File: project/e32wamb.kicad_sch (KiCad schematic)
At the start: 29 parts, among them J1 2060-452_998-404, J2 Conn_01x04, J3 Conn_01x03, Q1 AO3400, Q2 AO3400, Q3 AO3400, Q4 AO3400, Q5 AO3400, SW1 TS-1187A-B-A-B, U1 AP63203WU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

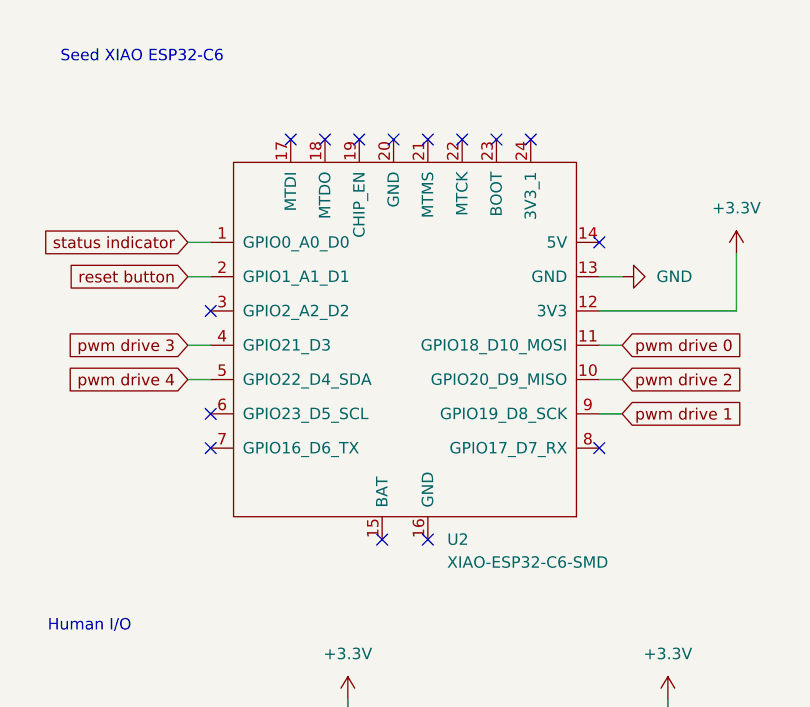
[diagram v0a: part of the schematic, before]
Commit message: Update xiao (don't place, add ds+source)
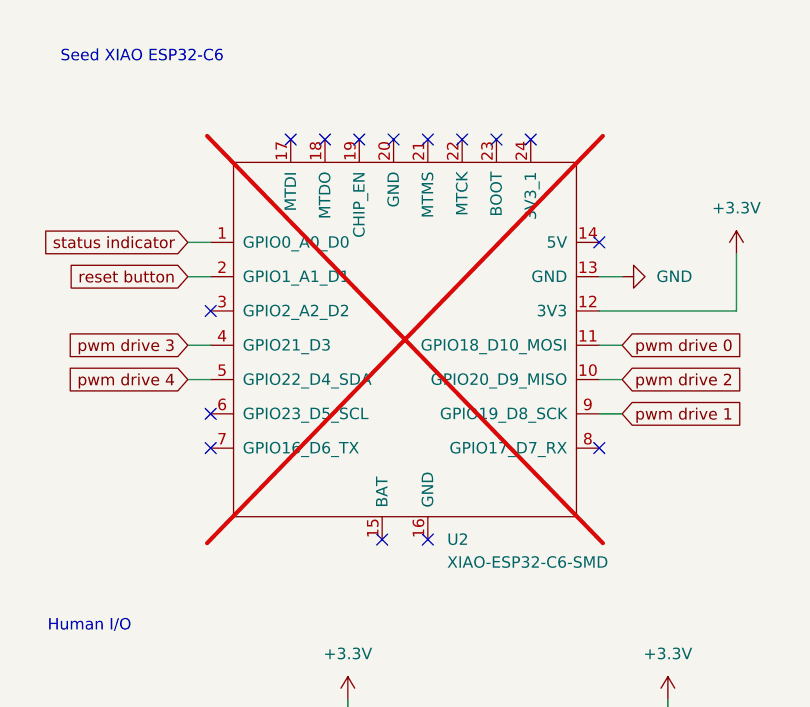
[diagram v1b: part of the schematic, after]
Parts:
- U2: Source (none) -> https://www.seeedstudio.com/Seeed-Studio-XIAO-ESP32C6-p-588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; now not fitted
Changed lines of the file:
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@@
 		(in_bom yes)
 		(on_board yes)
-		(dnp no)
+		(dnp yes)
 		(fields_autoplaced yes)
 		(property "Reference" "U2"
@@
 			)
 		)
-		(property "Datasheet" ""
+		(property "Datasheet" "https://files.seeedstudio.com/wiki/SeeedStudio-XIAO-ESP32C6/res/esp32-c6_datasheet_en.pdf"
 			(at 223.52 46.99 0)
 			(effects
@@
 			(at 232.41 52.07 0)
 			(effects
+				(font
+					(size 1.27 1.27)
+				)
+				(hide yes)
+			)
+		)
+		(property "Source" "https://www.seeedstudio.com/Seeed-Studio-XIAO-ESP32C6-p-5884.html"
+			(at 232.41 52.07 0)
+			(effects

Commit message: Add ohm symbol to all Rs, add license info
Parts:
- R1: value 10K -> 10kΩ
- R10, R12, R4, R6, R8: value 10k -> 10kΩ
- R11, R3, R5, R7, R9: value 390 -> 390Ω
- R2: value 0 -> 0Ω
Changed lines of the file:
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@@
 		(date "2025-04-05")
 		(company "wejn.org")
+		(comment 1 "Licensed under CC BY-SA 4.0")
+		(comment 2 "Open Source Hardware")
 	)
 	(text "Human I/O"
@@
 			)
 		)
-		(property "Value" "0"
+		(property "Value" "0Ω"
 			(at 213.36 96.52 90)
 			(effects
@@
 			)
 		)
-		(property "Value" "10k"
+		(property "Value" "10kΩ"
 			(at 35.56 144.7799 0)
 			(effects
@@
 			)
 		)
-		(property "Value" "390"
+		(property "Value" "390Ω"
 			(at 74.93 96.5199 0)
 			(effects
@@
 			)
 		)
-		(property "Value" "10k"
+		(property "Value" "10kΩ"
 			(at 35.56 105.4099 0)
 			(effects
@@
 			)
 		)
-		(property "Value" "10k"
+		(property "Value" "10kΩ"
 			(at 74.93 144.7799 0)
 			(effects
@@
 			)
 		)
-		(property "Value" "10K"
+		(property "Value" "10kΩ"
 			(at 264.16 97.7899 0)
 			(effects
@@
 			)
 		)
-		(property "Value" "10k"
+		(property "Value" "10kΩ"
 			(at 36.83 185.4199 0)
 			(effects
@@
 			)
 		)
-		(property "Value" "390"
+		(property "Value" "390Ω"
 			(at 36.83 175.2599 0)
 			(effects
@@
 			)
 		)
-		(property "Value" "390"
+		(property "Value" "390Ω"
 			(at 35.56 95.2499 0)
 			(effects
@@
 			)
 		)
-		(property "Value" "390"
+		(property "Value" "390Ω"
 			(at 74.93 134.6199 0)
 			(effects
@@
 			)
 		)
-		(property "Value" "390"
+		(property "Value" "390Ω"
 			(at 35.56 134.6199 0)
 			(effects
@@
 			)
 		)
-		(property "Value" "10k"
+		(property "Value" "10kΩ"
 			(at 74.93 106.6799 0)
 			(effects

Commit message: Add 3d models, smaller wago, mounting holes
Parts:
- added H1, H2: MountingHole_Pad, MountingHole:MountingHole_3.2mm_M3_Pad_TopBottom, symbol Mechanical:MountingHole_Pad
- J2: footprint Connector_JST:JST_PH_S4B-PH-SM4-TB_1x04-1MP_P2.00mm_Horizontal -> misc-lib:JST_PH_S4B-PH-SM4-TB_1x04-1MP_P2.00mm_Horizontal
- J3: footprint Connector_JST:JST_PH_S3B-PH-SM4-TB_1x03-1MP_P2.00mm_Horizontal -> misc-lib:JST_PH_S3B-PH-SM4-TB_1x03-1MP_P2.00mm_Horizontal
- SW1: footprint Button_Switch_SMD:SW_Push_1P1T_XKB_TS-1187A -> misc-lib:SW_Push_1P1T_XKB_TS-1187A
- U2: now fitted; now left out of the parts list
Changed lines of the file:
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@@
 			)
 		)
-		(property "Footprint" "Button_Switch_SMD:SW_Push_1P1T_XKB_TS-1187A"
+		(property "Footprint" "misc-lib:SW_Push_1P1T_XKB_TS-1187A"
 			(at 266.7 106.68 0)
 			(effects
@@
 	)
 	(symbol
+		(lib_id "Mechanical:MountingHole_Pad")
+		(at 121.92 172.72 0)
+		(unit 1)
+		(exclude_from_sim yes)
+		(in_bom no)
+		(on_board yes)
+		(dnp no)
+		(fields_autoplaced yes)
+		(property "Reference" "H2"
+			(at 124.46 170.1799 0)
+			(effects
+				(font
+					(size 1.27 1.27)
+				)
+				(justify left)
+			)
+		)
+		(property "Value" "MountingHole_Pad"
+			(at 124.46 172.7199 0)
+			(effects
+				(font
+					(size 1.27 1.27)
+				)
+				(justify left)
+			)
+		)
+		(property "Footprint" "MountingHole:MountingHole_3.2mm_M3_Pad_TopBottom"
+			(at 121.92 172.72 0)
+			(effects
+				(font
+					(size 1.27 1.27)
+				)
+				(hide yes)
+			)
+		)
+		(property "Datasheet" "~"
+			(at 121.92 172.72 0)
+			(effects
+				(font
+					(size 1.27 1.27)
+				)
+				(hide yes)
+			)
+		)
+		(property "Description" "Mounting Hole with connection"
+			(at 121.92 172.72 0)
+			(effects
+				(font
+					(size 1.27 1.27)
+				)
+				(hide yes)
+			)
+		)
+		(pin "1"
+		)
+		(instances
+			(project ""
+				(path "/982f5c8d-806c-4a7a-88bf-dbecf0057372"
+					(reference "H2")
+					(unit 1)
+				)
+			)
+		)
+	)
+	(symbol
 		(lib_id "power:+3.3V")
 		(at 269.24 41.91 0)
@@
 	)
 	(symbol
+		(lib_id "Mechanical:MountingHole_Pad")
+		(at 121.92 165.1 0)
+		(unit 1)
+		(exclude_from_sim yes)
+		(in_bom no)
+		(on_board yes)
+		(dnp no)
+		(fields_autoplaced yes)
+		(property "Reference" "H1"
+			(at 124.46 162.5599 0)
+			(effects
+				(font
+					(size 1.27 1.27)
+				)
+				(justify left)
+			)
+		)
+		(property "Value" "MountingHole_Pad"
+			(at 124.46 165.0999 0)
+			(effects
+				(font
+					(size 1.27 1.27)
+				)
+				(justify left)
+			)
+		)
+		(property "Footprint" "MountingHole:MountingHole_3.2mm_M3_Pad_TopBottom"
+			(at 121.92 165.1 0)
+			(effects
+				(font
+					(size 1.27 1.27)
+				)
+				(hide yes)
+			)
+		)
+		(property "Datasheet" "~"
+			(at 121.92 165.1 0)
+			(effects
+				(font
+					(size 1.27 1.27)
+				)
+				(hide yes)
+			)
+		)
+		(property "Description" "Mounting Hole with connection"
+			(at 121.92 165.1 0)
+			(effects
+				(font
+					(size 1.27 1.27)
+				)
+				(hide yes)
+			)
+		)
+		(pin "1"
+		)
+		(instances
+			(project ""
+				(path "/982f5c8d-806c-4a7a-88bf-dbecf0057372"
+					(reference "H1")
+					(unit 1)
+				)
+			)
+		)
+	)
+	(symbol
 		(lib_id "power:GND")
 		(at 41.91 148.59 0)
@@
 			)
 		)
-		(property "Footprint" "Connector_JST:JST_PH_S4B-PH-SM4-TB_1x04-1MP_P2.00mm_Horizontal"
+		(property "Footprint" "misc-lib:JST_PH_S4B-PH-SM4-TB_1x04-1MP_P2.00mm_Horizontal"
 			(at 133.35 130.81 0)
 			(effects
@@
 		(unit 1)
 		(exclude_from_sim no)
-		(in_bom yes)
+		(in_bom no)
 		(on_board yes)
-		(dnp yes)
+		(dnp no)
 		(fields_autoplaced yes)
 		(property "Reference" "U2"
@@
 			)
 		)
-		(property "Footprint" "Connector_JST:JST_PH_S3B-PH-SM4-TB_1x03-1MP_P2.00mm_Horizontal"
+		(property "Footprint" "misc-lib:JST_PH_S3B-PH-SM4-TB_1x03-1MP_P2.00mm_Horizontal"
 			(at 133.35 151.13 0)
 			(effects

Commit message: Flip connector, fix mosfet type and footprint
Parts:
- removed J1: 2060-452_998-404, wago-connector:2060452998404, symbol wago:2060-452_998-404
- added J1: 2059-302_998-403, 2059302998403, symbol wago2059:2059-302_998-403
- H1: footprint MountingHole:MountingHole_3.2mm_M3_Pad_TopBottom -> MountingHole:MountingHole_3.2mm_M3_ISO14580_Pad
- Q1, Q2, Q3, Q4, Q5: footprint Package_TO_SOT_SMD:SOT-23-3 -> Package_TO_SOT_SMD:SOT-23; symbol Simulation_SPICE:NMOS -> Transistor_FET:Q_NMOS_GSD
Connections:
- net GND: now also H1.1, H2.1, Q1.2 (S), Q2.2 (S), Q3.2 (S), Q4.2 (S), Q5.2 (S), J1.1 (1.1), J1.2 (1.2); no longer Q1.3 (S), Q2.3 (S), Q3.3 (S), Q4.3 (S), Q5.3 (S)
- net VIN: now also J3.3 (Pin_3), J1.3 (2.1), J1.4 (2.2); no longer J3.1 (Pin_1)
- net led 0: now also Q1.3 (D); no longer Q1.1 (D)
- net led 1: now also Q2.3 (D); no longer Q2.1 (D)
- net led 2: now also Q3.3 (D); no longer Q3.1 (D)
- net led 3: now also J3.1 (Pin_1), Q4.3 (D); no longer J3.2 (Pin_2), Q4.1 (D)
- net led 4: now also J3.2 (Pin_2), Q5.3 (D); no longer J3.3 (Pin_3), Q5.1 (D)
- net at R5.1: now also Q2.1 (G); no longer Q2.2 (G)
- net at R11.1: now also Q5.1 (G); no longer Q5.2 (G)
- net at R3.1: now also Q1.1 (G); no longer Q1.2 (G)
- net at R9.1: now also Q4.1 (G); no longer Q4.2 (G)
- net at R7.1: now also Q3.1 (G); no longer Q3.2 (G)
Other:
- moved on the sheet: H2

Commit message: Fix mounting hole h2 footprint
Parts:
- H2: footprint MountingHole:MountingHole_3.2mm_M3_Pad_TopBottom -> MountingHole:MountingHole_3.2mm_M3_ISO14580_Pad
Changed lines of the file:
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@@
 	(title_block
 		(title "e32wamb pcb")
-		(date "2025-04-06")
-		(rev "2")
+		(date "2025-04-08")
+		(rev "1")
 		(company "wejn.org")
 		(comment 1 "Licensed under CC BY-SA 4.0")
@@
 			)
 		)
-		(property "Footprint" "MountingHole:MountingHole_3.2mm_M3_Pad_TopBottom"
+		(property "Footprint" "MountingHole:MountingHole_3.2mm_M3_ISO14580_Pad"
 			(at 121.92 179.07 0)
 			(effects

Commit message: Add lcsc part number for smaller wago
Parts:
- J1: LCSC (none) -> C2765060
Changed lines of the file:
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@@
+			)
+		)
+		(property "LCSC" "C2765060"
+			(at 119.38 100.33 0)
+			(effects
+				(font
+					(size 1.27 1.27)
+				)
+				(hide yes)
 			)
 		)

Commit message: Oops: c2,c3 were wrong footprint (lcsc num)
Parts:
- C2, C3: LCSC C12891 -> C59461
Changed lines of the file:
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@@
 			)
 		)
-		(property "LCSC" "C12891"
+		(property "LCSC" "C59461"
 			(at 92.71 46.99 0)
 			(effects
@@
 			)
 		)
-		(property "LCSC" "C12891"
+		(property "LCSC" "C59461"
 			(at 81.28 46.99 0)
 			(effects

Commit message: Add rotation offset for U1 (for jlcfab), bump revision
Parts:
- U1: FT Rotation Offset (none) -> 90
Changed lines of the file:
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@@
 	(title_block
 		(title "e32wamb pcb")
-		(date "2025-04-08")
-		(rev "1")
+		(date "2025-04-09")
+		(rev "2")
 		(company "wejn.org")
 		(comment 1 "Licensed under CC BY-SA 4.0")
@@
 			(at 46.99 43.18 0)
 			(effects
+				(font
+					(size 1.27 1.27)
+				)
+				(hide yes)
+			)
+		)
+		(property "FT Rotation Offset" "90"
+			(at 46.99 43.18 0)
+			(effects
